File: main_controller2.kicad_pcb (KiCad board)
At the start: 4 copper layers, 214.6 x 96.5 mm, 80 parts, among them J1 xt30, J10 Conn_01x04, J11 Conn_01x04, J12 Conn_01x04, J13 Conn_01x04, J2 Conn_01x04, J3 xt30, J4 Conn_01x08, J8 SMA, J9 Conn_01x04, Q1 FDN359BN, SW1 SW_SPST, SW2 SW_SPST, U1 ESP32-WROOM-32D, U10 BTN7030-1EPA, U11 PCA9557PW, U12 RFM95W-915S2, U13 W25N02KVZEIR, U14 MCP2517FD-xSL, U15 SN65HVD230, U2 BMI088, U3 china_buck_converter, U4 AP7361-33ER-13, U5 MS5611-01BA, U6 BTS70802, U7 BTN7030-1EPA, U8 BTN7030-1EPA, U9 BTN7030-1EPA, Y1 40MHz

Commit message: stackable version
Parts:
- removed C15: 0.1u, Capacitor_SMD:C_0603_1608Metric
- removed J11, J12, J13, J2: Conn_01x04, Connector_JST:JST_XH_B4B-XH-A_1x04_P2.50mm_Vertical
- removed JP3, JP4: SolderJumper_2_Open, Jumper:SolderJumper-2_P1.3mm_Open_TrianglePad1.0x1.5mm
- removed REF**: PinHeader_1x12_P2.54mm_Vertical, Connector_PinHeader_2.54mm:PinHeader_1x12_P2.54mm_Vertical
- removed REF**: PinHeader_1x20_P1.27mm_Vertical, Connector_PinHeader_1.27mm:PinHeader_1x20_P1.27mm_Vertical
- removed REF**: PinHeader_2x15_P1.27mm_Vertical, Connector_PinHeader_1.27mm:PinHeader_2x15_P1.27mm_Vertical
- removed REF** (x2): MountingHole_2.2mm_M2_Pad_Via, MountingHole:MountingHole_2.2mm_M2_Pad_Via
- removed U12: RFM95W-915S2, RF_Module:HOPERF_RFM9XW_SMD
- added J6: Conn_01x02, Connector_JST:JST_XH_S2B-XH-A_1x02_P2.50mm_Horizontal, F.Cu at (229.2, 145.4)
- added J7: Conn_01x02, Connector_JST:JST_XH_S2B-XH-A_1x02_P2.50mm_Horizontal, F.Cu at (220.6, 145.4)
- added R11: 2k2, Resistor_SMD:R_0603_1608Metric, F.Cu at (277.1, 150.4)
- added R12: 2k2, Resistor_SMD:R_0603_1608Metric, F.Cu at (286.4, 107.7)
- BZ1, U11: moved to F.Cu
- C10, U10, U6, U7, U8, U9: moved to B.Cu
- C5: value big -> edda_cap
- D1, D2: footprint LED_SMD:LED_WS2812B_PLCC4_5.0x5.0mm_P3.2mm -> LED_SMD:LED_WS2812B-2020_PLCC4_2.0x2.0mm; moved to B.Cu
- J10: value Conn_01x04 -> Conn_01x15; footprint Connector_JST:JST_XH_B4B-XH-A_1x04_P2.50mm_Vertical -> Connector_PinHeader_2.54mm:PinHeader_1x15_P2.54mm_Vertical
- J4: value Conn_01x08 -> Conn_01x02; footprint TerminalBlock_RND:TerminalBlock_RND_205-00007_1x08_P5.00mm_Horizontal -> Connector_JST:JST_XH_S2B-XH-A_1x02_P2.50mm_Horizontal
- J8: value SMA -> Conn_01x02; footprint Connector_Coaxial:SMA_Molex_73251-1153_EdgeMount_Horizontal -> Connector_JST:JST_XH_S2B-XH-A_1x02_P2.50mm_Horizontal; moved to F.Cu
- J9: value Conn_01x04 -> Conn_01x16; footprint Connector_JST:JST_XH_B4B-XH-A_1x04_P2.50mm_Vertical -> Connector_PinHeader_2.54mm:PinHeader_1x16_P2.54mm_Vertical
- JP1: footprint Connector_JST:JST_XH_B2B-XH-A_1x02_P2.50mm_Vertical -> Connector_JST:JST_XH_S2B-XH-A_1x02_P2.50mm_Horizontal
- JP2: footprint Connector_AMASS:AMASS_XT30UPB-F_1x02_P5.0mm_Vertical -> Connector_AMASS:AMASS_XT30PW-F_1x02_P2.50mm_Horizontal
- U1: value ESP32-WROOM-32D -> ESP32-PICO-MINI-02; footprint RF_Module:ESP32-WROOM-32 -> lib:MODULE_ESP32-PICO-MINI-02U
- U13: footprint Package_SO:SOIC-8_5.275x5.275mm_P1.27mm -> lib:SON127P800X600X80-9N-D; moved to F.Cu
- moved J4 211.3 mm to (237.8, 145.4), turned to 0 degrees
- moved U7 200.0 mm to (239.0, 138.7), turned to -90 degrees
- moved U9 189.5 mm to (230.4, 138.7), turned to -90 degrees
- moved J8 185.0 mm to (211.9, 145.4), turned to 0 degrees
- moved BZ1 183.3 mm to (238.3, 136.9), turned to 0 degrees
- moved U8 179.2 mm to (221.7, 138.7), turned to -90 degrees
- moved C5 176.3 mm to (236.7, 111.8), turned to 180 degrees
- moved J3 176.2 mm to (218.3, 106.5), turned to 0 degrees
- moved U4 174.8 mm to (222.6, 115.1), turned to 180 degrees
- moved JP2 172.0 mm to (232.8, 106.5), turned to 0 degrees
- moved U3 171.5 mm to (222.3, 127.0), turned to -90 degrees
- moved U10 169.0 mm to (213.2, 138.5), turned to -90 degrees
- moved H3 167.6 mm to (245.9, 100.9)
- moved U11 165.5 mm to (230.2, 127.8), turned to 180 degrees
- moved U13 165.4 mm to (219.5, 128.3), turned to -90 degrees
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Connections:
- C9 pad 1: +5V -> Earth
- C9 pad 2: Earth -> +5V
- D1 pad 1: +5V -> +3V3
- D2 pad 1: +5V -> +3V3
- J10 pad 1: Earth -> /GND
- J10 pad 2: /TM_RX -> /GND
- J10 pad 3: /TM_TX -> VCC
- J10 pad 4: +5V -> VCC
- J4 pad 1: /PYRO_1 -> Earth
- J4 pad 2: Earth -> /PYRO_1
- J8 pad 1: Net-(U12-Pad9) -> Earth
- J8 pad 2: Earth -> /PYRO_4
- J9 pad 1: Earth -> /GND
- J9 pad 2: /GPS2_RX -> /RX0
- J9 pad 3: /GPS2_TX -> /TX0
- J9 pad 4: +5V -> /RX1
- Q1 pad 1: /BUZZER -> /BOOTLOADER
- R6 pad 1: /SDA -> /SDA0
- R7 pad 1: /SCL -> /SCL0
- U1 pad 10: /PYRO_1 -> /RX1
- U1 pad 11: /PYRO_2 -> Earth
- U1 pad 12: /CAN_CS -> /TX1
- U1 pad 13: /HSPI_SCK -> /TX2
- U1 pad 14: /HSPI_MISO -> Earth
- U1 pad 15: Earth -> /LED_RMT
- U1 pad 16: /HSPI_MOSI -> /SDA1
- U1 pad 17: unconnected-(U1-Pad17) -> /SCL1
- U1 pad 18: unconnected-(U1-Pad18) -> /HSPI_SCK
- U1 pad 19: unconnected-(U1-Pad19) -> /HSPI_MISO
- U1 pad 2: +3V3 -> Earth
- U1 pad 20: unconnected-(U1-Pad20) -> /HSPI_MOSI
- U1 pad 21: unconnected-(U1-Pad21) -> /MISC_IO1
- U1 pad 22: unconnected-(U1-Pad22) -> /SDA0
- U1 pad 23: /BUZZER -> /BOOTLOADER
- U1 pad 24: /LED_TX -> /SCL0
- U1 pad 25: /BOOTLOADER -> unconnected-(U1-Pad25)
- U1 pad 26: /GPS_TX -> /PYRO_2
- U1 pad 27: /GPS2_TX -> /VSPI_MOSI
- U1 pad 28: /GPS2_RX -> /VSPI_SCK
- U1 pad 29: /GPS_RX -> /MISC_IO0
- U1 pad 3: Net-(R8-Pad2) -> +3V3
- U1 pad 30: /VSPI_SCK -> /RX0
- U1 pad 31: /VSPI_MISO -> /TX0
- U1 pad 33: /SDA -> /PYRO_1
- U1 pad 34: /TELEM_RX -> /FLASH_CS
- U1 pad 35: /TELEM_TX -> /CAN_CS
- U1 pad 36: /SCL -> Earth
- U1 pad 37: /VSPI_MOSI -> Earth
- U1 pad 4: /VBAT_SENSE -> /VSPI_MISO
- U1 pad 5: /CURR_SENSE -> /VBAT_SENSE
- U1 pad 6: /CAN_IRQ -> /CURR_SENSE
- U1 pad 7: unconnected-(U1-Pad7) -> /CAN_IRQ
- U1 pad 8: /FLASH_CS -> Net-(R8-Pad2)
- U1 pad 9: /LORA_CS -> /RX2
- U11 pad 10: /LORA_RESET -> /EDDA_EN
- U11 pad 11: /CURR_EN -> /CURR_SEL
- U11 pad 12: /EDDA_EN -> /MISC_IO2
- U11 pad 13: /CURR_SEL -> /MISC_IO3
- U11 pad 14: /CAN_MISC_PIN -> unconnected-(U11-Pad14)
- U14 pad 10: /VSPI_SCK -> /HSPI_SCK
- U14 pad 11: /VSPI_MOSI -> /HSPI_MOSI
- U14 pad 12: /VSPI_MISO -> /HSPI_MISO
- U14 pad 14: unconnected-(U14-Pad14) -> +3V3
- U14 pad 7: unconnected-(U14-Pad7) -> Earth
- U15 pad 5: /CAN_MISC_PIN -> +3V3
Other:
- board size 214.6 x 96.5 mm -> 213.9 x 95.8 mm

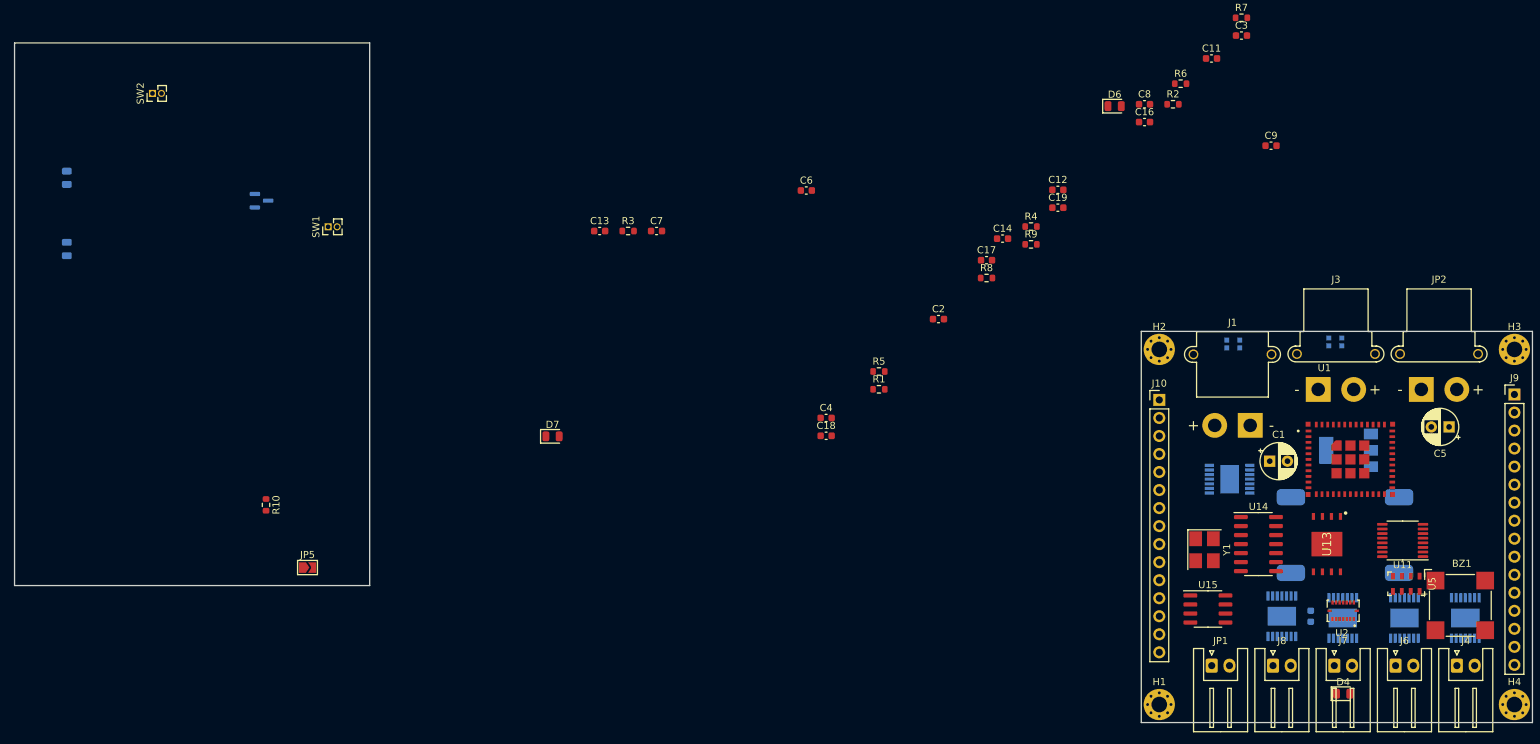
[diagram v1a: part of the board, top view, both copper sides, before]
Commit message: move to esp pico
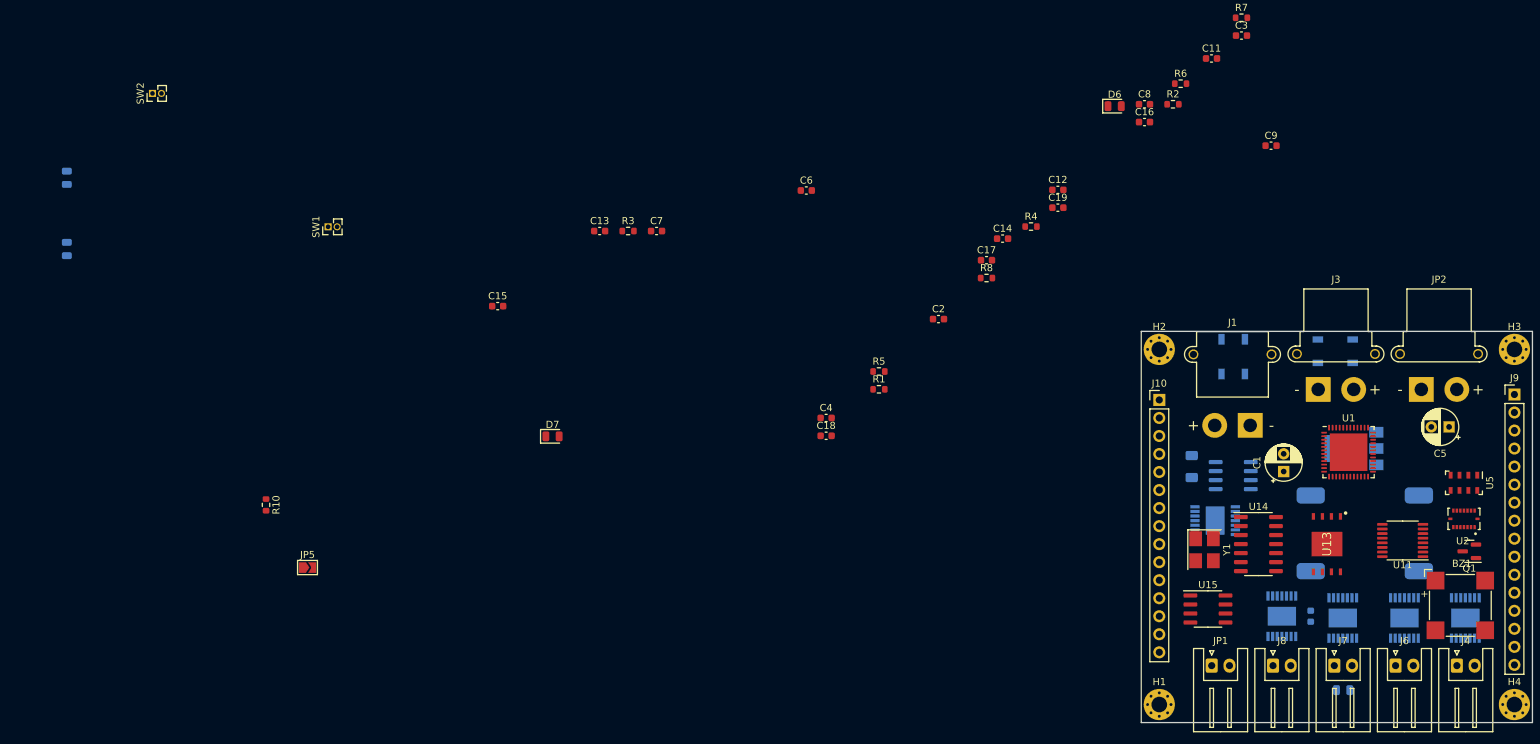
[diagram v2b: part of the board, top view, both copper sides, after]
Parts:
- added C15: 0.1u, Capacitor_SMD:C_0603_1608Metric, F.Cu at (102.7, 94.8)
- added U12: INA219AxD, Package_SO:SOIC-8_3.9x4.9mm_P1.27mm, B.Cu at (206.3, 118.6)
- D1, D2: footprint LED_SMD:LED_WS2812B-2020_PLCC4_2.0x2.0mm -> LED_SMD:LED_WS2812B_PLCC4_5.0x5.0mm_P3.2mm
- D4: moved to B.Cu
- Q1: moved to F.Cu
- R9: value 300 -> R; footprint Resistor_SMD:R_0603_1608Metric -> Resistor_SMD:R_1206_3216Metric_Pad1.30x1.75mm_HandSolder; moved to B.Cu
- U1: value ESP32-PICO-MINI-02 -> ESP32-PICO-D4; footprint lib:MODULE_ESP32-PICO-MINI-02U -> Package_DFN_QFN:QFN-48-1EP_7x7mm_P0.5mm_EP5.3x5.3mm
- moved Q1 177.2 mm to (239.6, 129.3), turned to 180 degrees
- moved R9 38.6 mm to (200.5, 117.4), turned to -90 degrees
- moved U2 21.4 mm to (238.8, 124.7)
- moved U5 16.4 mm to (238.8, 119.7)
- moved U6 6.19 mm to (203.8, 125.0)
- moved U3 2.81 mm to (225.1, 126.8)
- moved C1 2.45 mm to (213.4, 118.1), turned to 90 degrees
- moved D2 1.78 mm to (206.3, 101.9), turned to -90 degrees
- moved D1 1.31 mm to (220.7, 101.1)
- moved U1 1.05 mm to (222.6, 115.3)
- moved U4 0.80 mm to (223.3, 114.8)
- moved D4 0.51 mm to (221.8, 148.9)
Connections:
- J1 pad 2: +BATT -> Net-(J1-Pad2)
- Q1 pad 1: /BOOTLOADER -> /BUZZER
- R1 pad 1: +BATT -> Net-(J1-Pad2)
- R9 pad 1: /CURR_EN -> Net-(J1-Pad2)
- R9 pad 2: Earth -> +BATT
- U1 pad 1: Earth -> Net-(U1-Pad1)
- U1 pad 10: /RX1 -> /VSPI_MISO
- U1 pad 11: Earth -> /CAN_IRQ
- U1 pad 12: /TX1 -> /SDA0
- U1 pad 13: /TX2 -> /SCL0
- U1 pad 14: Earth -> /SCL1
- U1 pad 15: /LED_RMT -> /TX1
- U1 pad 16: /SDA1 -> /TX2
- U1 pad 17: /SCL1 -> /HSPI_SCK
- U1 pad 18: /HSPI_SCK -> /HSPI_MISO
- U1 pad 19: /HSPI_MISO -> unconnected-(U1-Pad19)
- U1 pad 2: Earth -> unconnected-(U1-Pad2)
- U1 pad 21: /MISC_IO1 -> /PYRO_1
- U1 pad 22: /SDA0 -> /MISC_IO0
- U1 pad 24: /SCL0 -> /MISC_IO0
- U1 pad 26: /PYRO_2 -> +3V3
- U1 pad 27: /VSPI_MOSI -> unconnected-(U1-Pad27)
- U1 pad 29: /MISC_IO0 -> /MISC_IO1
- U1 pad 3: +3V3 -> Net-(U1-Pad3)
- U1 pad 30: /RX0 -> unconnected-(U1-Pad30)
- U1 pad 31: /TX0 -> unconnected-(U1-Pad31)
- U1 pad 33: /PYRO_1 -> unconnected-(U1-Pad33)
- U1 pad 34: /FLASH_CS -> /VSPI_MOSI
- U1 pad 35: /CAN_CS -> /PYRO_2
- U1 pad 36: Earth -> /SDA1
- U1 pad 37: Earth -> unconnected-(U1-Pad37)
- U1 pad 38: Earth -> /CAN_CS
- U1 pad 39: Earth -> /LED_RMT
- U1 pad 4: /VSPI_MISO -> Net-(U1-Pad3)
- U1 pad 40: Earth -> /RX0
- U1 pad 41: Earth -> /TX0
- U1 pad 42: Earth -> /FLASH_CS
- U1 pad 43: Earth -> Net-(U1-Pad1)
- U1 pad 44: Earth -> unconnected-(U1-Pad44)
- U1 pad 45: Earth -> unconnected-(U1-Pad45)
- U1 pad 46: Earth -> Net-(U1-Pad1)
- U1 pad 47: Earth -> unconnected-(U1-Pad47)
- U1 pad 48: Earth -> unconnected-(U1-Pad48)
- U1 pad 49: Earth -> unconnected-(U1-Pad49)
- U1 pad 5: /VBAT_SENSE -> /RX2
- U1 pad 6: /CURR_SENSE -> /RX1
- U1 pad 7: /CAN_IRQ -> /CURR_SENSE
- U1 pad 8: Net-(R8-Pad2) -> /VBAT_SENSE
- U1 pad 9: /RX2 -> Net-(R8-Pad2)
- U11 pad 11: /CURR_SEL -> unconnected-(U11-Pad11)
- U6 pad 3: /CURR_EN -> unconnected-(U6-Pad3)
- U6 pad 4: /CURR_SENSE -> unconnected-(U6-Pad4)
- U6 pad 5: /CURR_SEL -> unconnected-(U6-Pad5)
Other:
- board size 213.9 x 95.8 mm -> 55.1 x 55.1 mm
